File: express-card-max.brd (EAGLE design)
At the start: 51.4 x 65 mm, 1 part

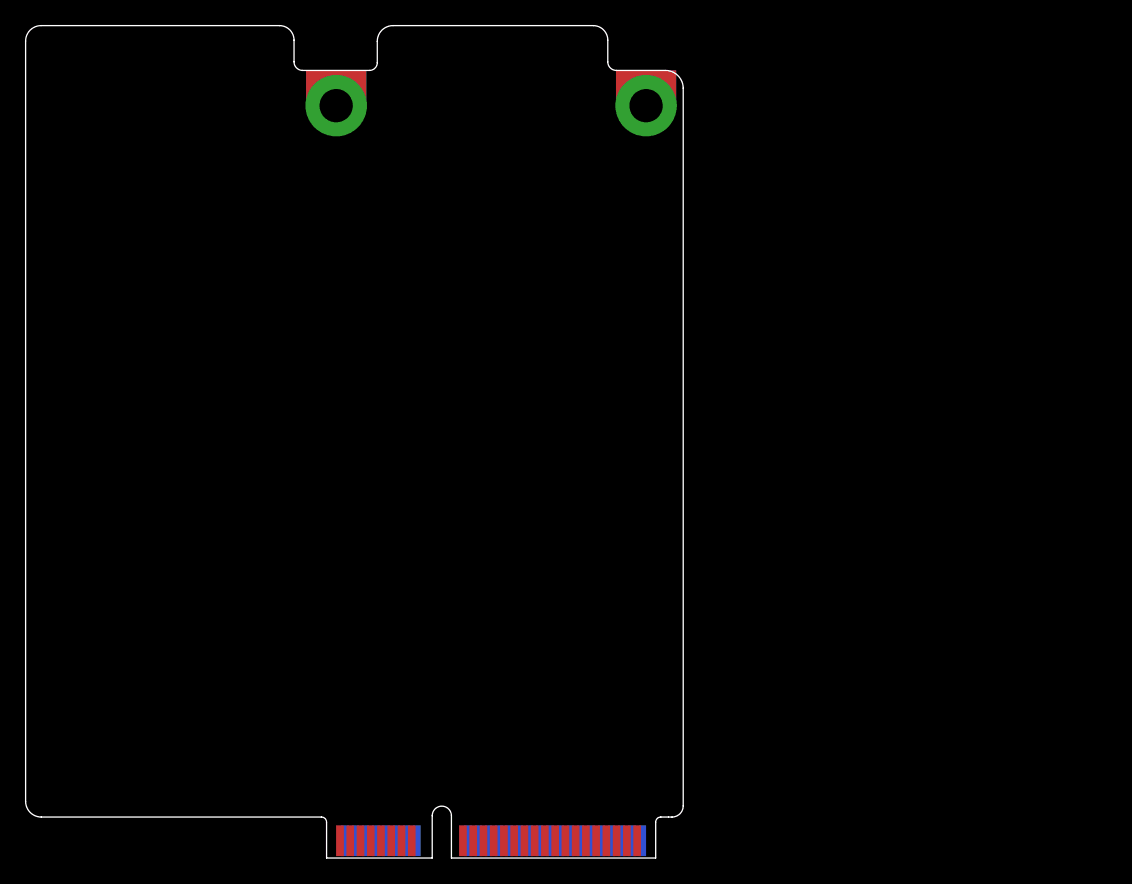
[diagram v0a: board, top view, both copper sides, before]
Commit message: board placement into positive values
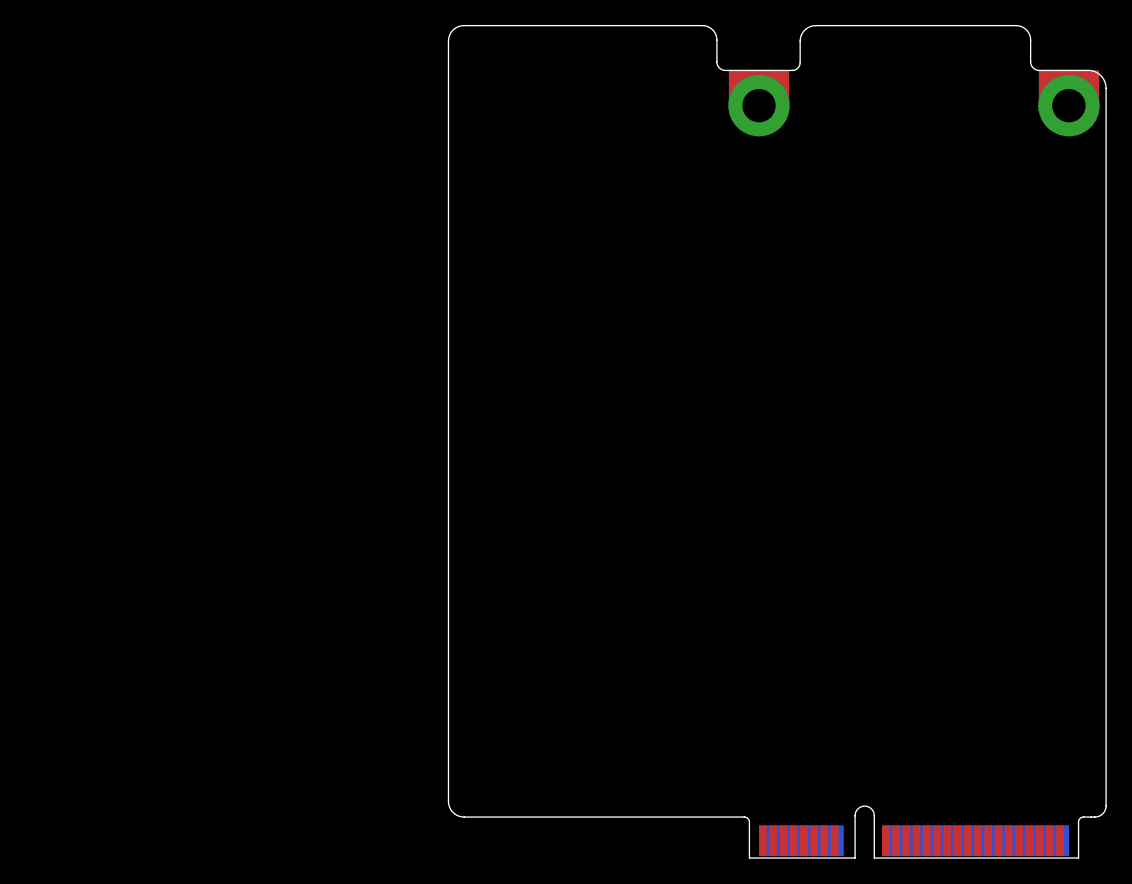
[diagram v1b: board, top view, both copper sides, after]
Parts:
- moved U$1 33.0 mm to (33.0, 0.00)
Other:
- board size 51.4 x 65 mm -> 51.3 x 65 mm
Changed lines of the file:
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@@
 <board>
 <plain>
-<wire x1="-0.75" y1="0.1" x2="-0.75" y2="3.4" width="0" layer="20"/>
-<wire x1="0.75" y1="0.1" x2="0.75" y2="3.4" width="0" layer="20"/>
-<wire x1="-0.75" y1="3.4" x2="0.75" y2="3.4" width="0" layer="20" curve="-180"/>
-<wire x1="-0.75" y1="0.1" x2="-9" y2="0.1" width="0" layer="20"/>
-<wire x1="-9" y1="0.1" x2="-9" y2="2.9" width="0" layer="20"/>
-<wire x1="-9.4" y1="3.3" x2="-31.279346875" y2="3.3" width="0" layer="20"/>
-<wire x1="-31.279346875" y1="3.3" x2="-32.5" y2="4.520653125" width="0" layer="20" curve="-90"/>
-<wire x1="-32.5" y1="4.520653125" x2="-32.5" y2="63.891696875" width="0" layer="20"/>
-<wire x1="-9.4" y1="3.3" x2="-9" y2="2.9" width="0" layer="20" curve="-90"/>
-<wire x1="18.85" y1="60.20985625" x2="18.85" y2="4.173209375" width="0" layer="20"/>
-<wire x1="18.85" y1="4.173209375" x2="17.976790625" y2="3.3" width="0" layer="20" curve="-90"/>
-<wire x1="17.976790625" y1="3.3" x2="17.7" y2="3.3" width="0" layer="20"/>
-<wire x1="0.75" y1="0.1" x2="16.7" y2="0.1" width="0" layer="20"/>
-<wire x1="16.7" y1="0.1" x2="16.7" y2="2.9" width="0" layer="20"/>
-<wire x1="17.7" y1="3.3" x2="17.1" y2="3.3" width="0" layer="20"/>
-<wire x1="17.1" y1="3.3" x2="16.7" y2="2.9" width="0" layer="20" curve="90"/>
-<wire x1="-32.5" y1="63.891696875" x2="-31.291696875" y2="65.1" width="0" layer="20" curve="-90"/>
-<wire x1="-31.291696875" y1="65.1" x2="-12.672075" y2="65.1" width="0" layer="20"/>
-<wire x1="-5.6495875" y1="61.6" x2="-5.04" y2="62.2095875" width="0" layer="20" curve="90"/>
-<wire x1="-5.04" y1="62.2095875" x2="-5.04" y2="63.874603125" width="0" layer="20"/>
-<wire x1="18.85" y1="60.20985625" x2="17.45985625" y2="61.6" width="0" layer="20" curve="90"/>
-<wire x1="12.96" y1="63.967925" x2="12.96" y2="62.272009375" width="0" layer="20"/>
-<wire x1="12.96" y1="62.272009375" x2="13.632009375" y2="61.6" width="0" layer="20" curve="90"/>
-<wire x1="13.632009375" y1="61.6" x2="17.45985625" y2="61.6" width="0" layer="20"/>
-<wire x1="-5.04" y1="63.874603125" x2="-3.814603125" y2="65.1" width="0" layer="20" curve="-90"/>
-<wire x1="-3.814603125" y1="65.1" x2="11.827925" y2="65.1" width="0" layer="20"/>
-<wire x1="11.827925" y1="65.1" x2="12.96" y2="63.967925" width="0" layer="20" curve="-90"/>
-<wire x1="-11.54" y1="63.967925" x2="-11.54" y2="62.272009375" width="0" layer="20"/>
-<wire x1="-11.54" y1="62.272009375" x2="-10.867990625" y2="61.6" width="0" layer="20" curve="90"/>
-<wire x1="-12.672075" y1="65.1" x2="-11.54" y2="63.967925" width="0" layer="20" curve="-90"/>
-<wire x1="-10.867990625" y1="61.6" x2="-5.6495875" y2="61.6" width="0" layer="20"/>
+<wire x1="32.27" y1="0.1" x2="32.27" y2="3.4" width="0" layer="20"/>
+<wire x1="33.77" y1="0.1" x2="33.77" y2="3.4" width="0" layer="20"/>
+<wire x1="32.27" y1="3.4" x2="33.77" y2="3.4" width="0" layer="20" curve="-180"/>
+<wire x1="32.27" y1="0.1" x2="24.02" y2="0.1" width="0" layer="20"/>
+<wire x1="24.02" y1="0.1" x2="24.02" y2="2.9" width="0" layer="20"/>
+<wire x1="23.62" y1="3.3" x2="1.740653125" y2="3.3" width="0" layer="20"/>
+<wire x1="1.740653125" y1="3.3" x2="0.52" y2="4.520653125" width="0" layer="20" curve="-90"/>
+<wire x1="0.52" y1="4.520653125" x2="0.52" y2="63.891696875" width="0" layer="20"/>
+<wire x1="23.62" y1="3.3" x2="24.02" y2="2.9" width="0" layer="20" curve="-90"/>
+<wire x1="51.87" y1="60.20985625" x2="51.87" y2="4.173209375" width="0" layer="20"/>
+<wire x1="51.87" y1="4.173209375" x2="50.996790625" y2="3.3" width="0" layer="20" curve="-90"/>
+<wire x1="50.996790625" y1="3.3" x2="50.72" y2="3.3" width="0" layer="20"/>
+<wire x1="33.77" y1="0.1" x2="49.72" y2="0.1" width="0" layer="20"/>
+<wire x1="49.72" y1="0.1" x2="49.72" y2="2.9" width="0" layer="20"/>
+<wire x1="50.72" y1="3.3" x2="50.12" y2="3.3" width="0" layer="20"/>
+<wire x1="50.12" y1="3.3" x2="49.72" y2="2.9" width="0" layer="20" curve="90"/>
+<wire x1="0.52" y1="63.891696875" x2="1.728303125" y2="65.1" width="0" layer="20" curve="-90"/>
+<wire x1="1.728303125" y1="65.1" x2="20.347925" y2="65.1" width="0" layer="20"/>
+<wire x1="27.3704125" y1="61.6" x2="27.98" y2="62.2095875" width="0" layer="20" curve="90"/>
+<wire x1="27.98" y1="62.2095875" x2="27.98" y2="63.874603125" width="0" layer="20"/>
+<wire x1="51.87" y1="60.20985625" x2="50.47985625" y2="61.6" width="0" layer="20" curve="90"/>
+<wire x1="45.98" y1="63.967925" x2="45.98" y2="62.272009375" width="0" layer="20"/>
+<wire x1="45.98" y1="62.272009375" x2="46.652009375" y2="61.6" width="0" layer="20" curve="90"/>
+<wire x1="46.652009375" y1="61.6" x2="50.47985625" y2="61.6" width="0" layer="20"/>
+<wire x1="27.98" y1="63.874603125" x2="29.205396875" y2="65.1" width="0" layer="20" curve="-90"/>
+<wire x1="29.205396875" y1="65.1" x2="44.847925" y2="65.1" width="0" layer="20"/>
+<wire x1="44.847925" y1="65.1" x2="45.98" y2="63.967925" width="0" layer="20" curve="-90"/>
+<wire x1="21.48" y1="63.967925" x2="21.48" y2="62.272009375" width="0" layer="20"/>
+<wire x1="21.48" y1="62.272009375" x2="22.152009375" y2="61.6" width="0" layer="20" curve="90"/>
+<wire x1="20.347925" y1="65.1" x2="21.48" y2="63.967925" width="0" layer="20" curve="-90"/>
+<wire x1="22.152009375" y1="61.6" x2="27.3704125" y2="61.6" width="0" layer="20"/>
 </plain>
 <attributes>
@@
 </autorouter>
 <elements>
-<element name="U$1" library="teensy-express" package="FULL-MINI-PCI-E" value="FULL-MINI-PCI-E" x="0" y="0"/>
+<element name="U$1" library="teensy-express" package="FULL-MINI-PCI-E" value="FULL-MINI-PCI-E" x="33.02" y="0"/>
 </elements>
 <signals>
@@
 <contactref element="U$1" pad="LATCH@1"/>
 <contactref element="U$1" pad="LATCH@2"/>
-<wire x1="-8.25" y1="58.85" x2="15.95" y2="58.85" width="0" layer="19" extent="1-1"/>
+<wire x1="24.77" y1="58.85" x2="48.97" y2="58.85" width="0" layer="19" extent="1-1"/>
 </signal>
 </signals>
